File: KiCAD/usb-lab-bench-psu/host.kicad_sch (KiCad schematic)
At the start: 23 parts, among them SW1 SW_Push, U3 ESP32-C3, U4 ZD25WQ32C, Y1 40MHz

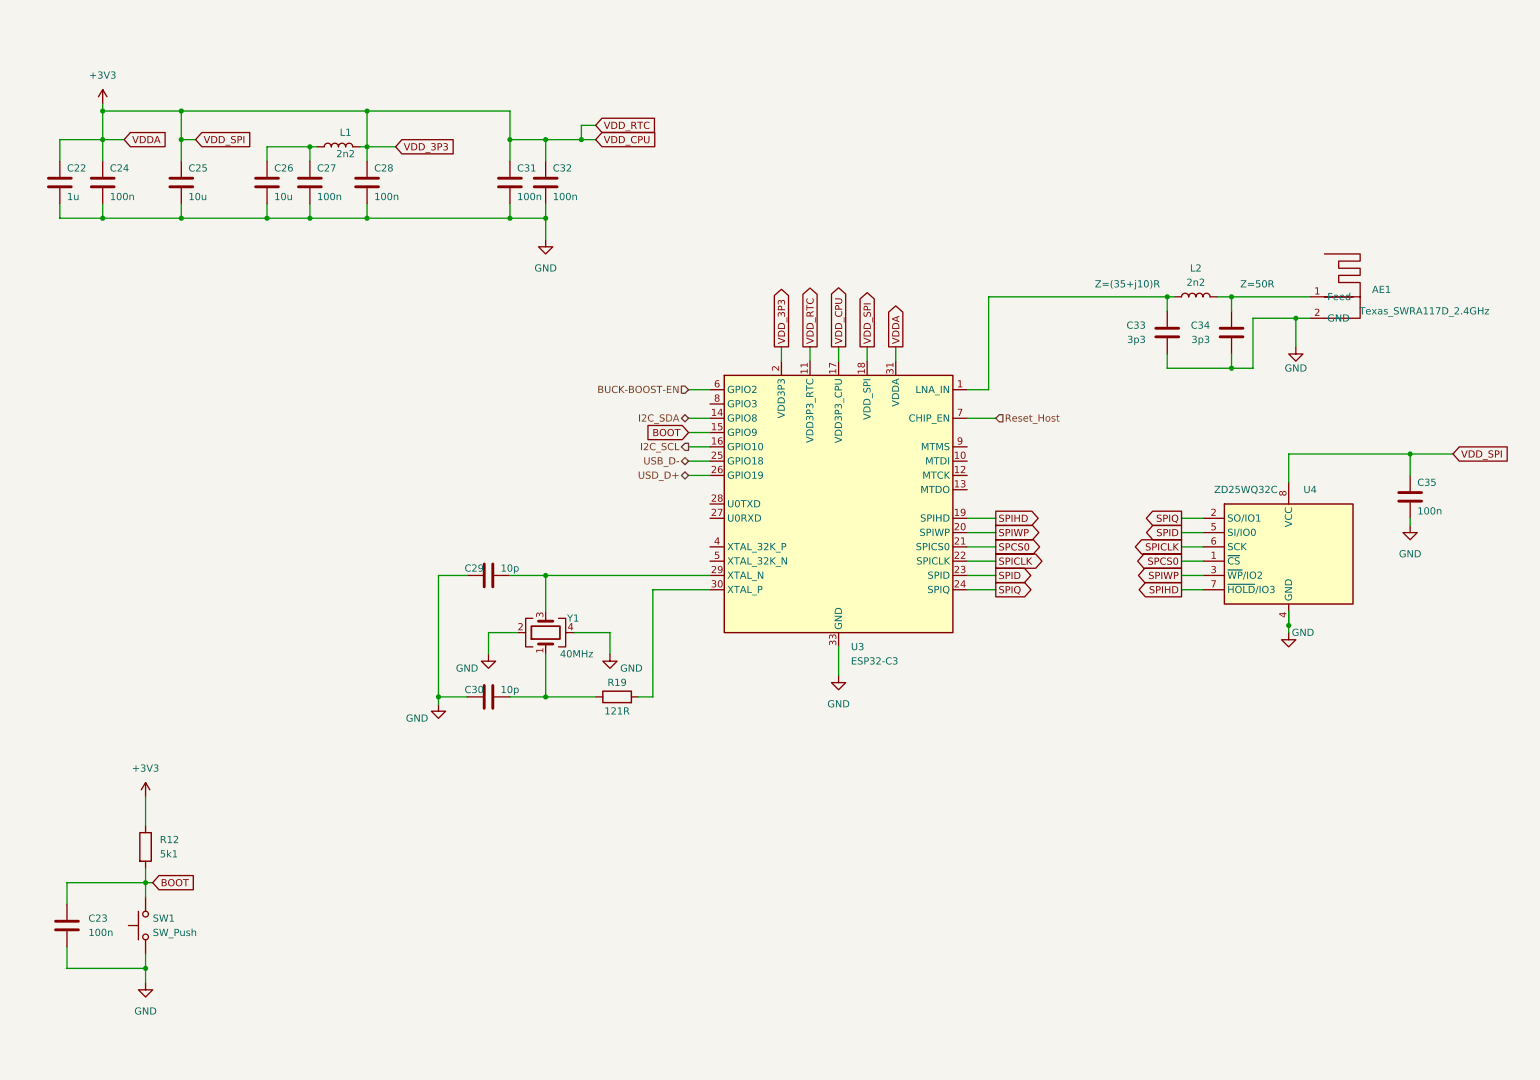
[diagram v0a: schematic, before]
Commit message: Replaced global labels with labels, added measurement circuit, started with io board
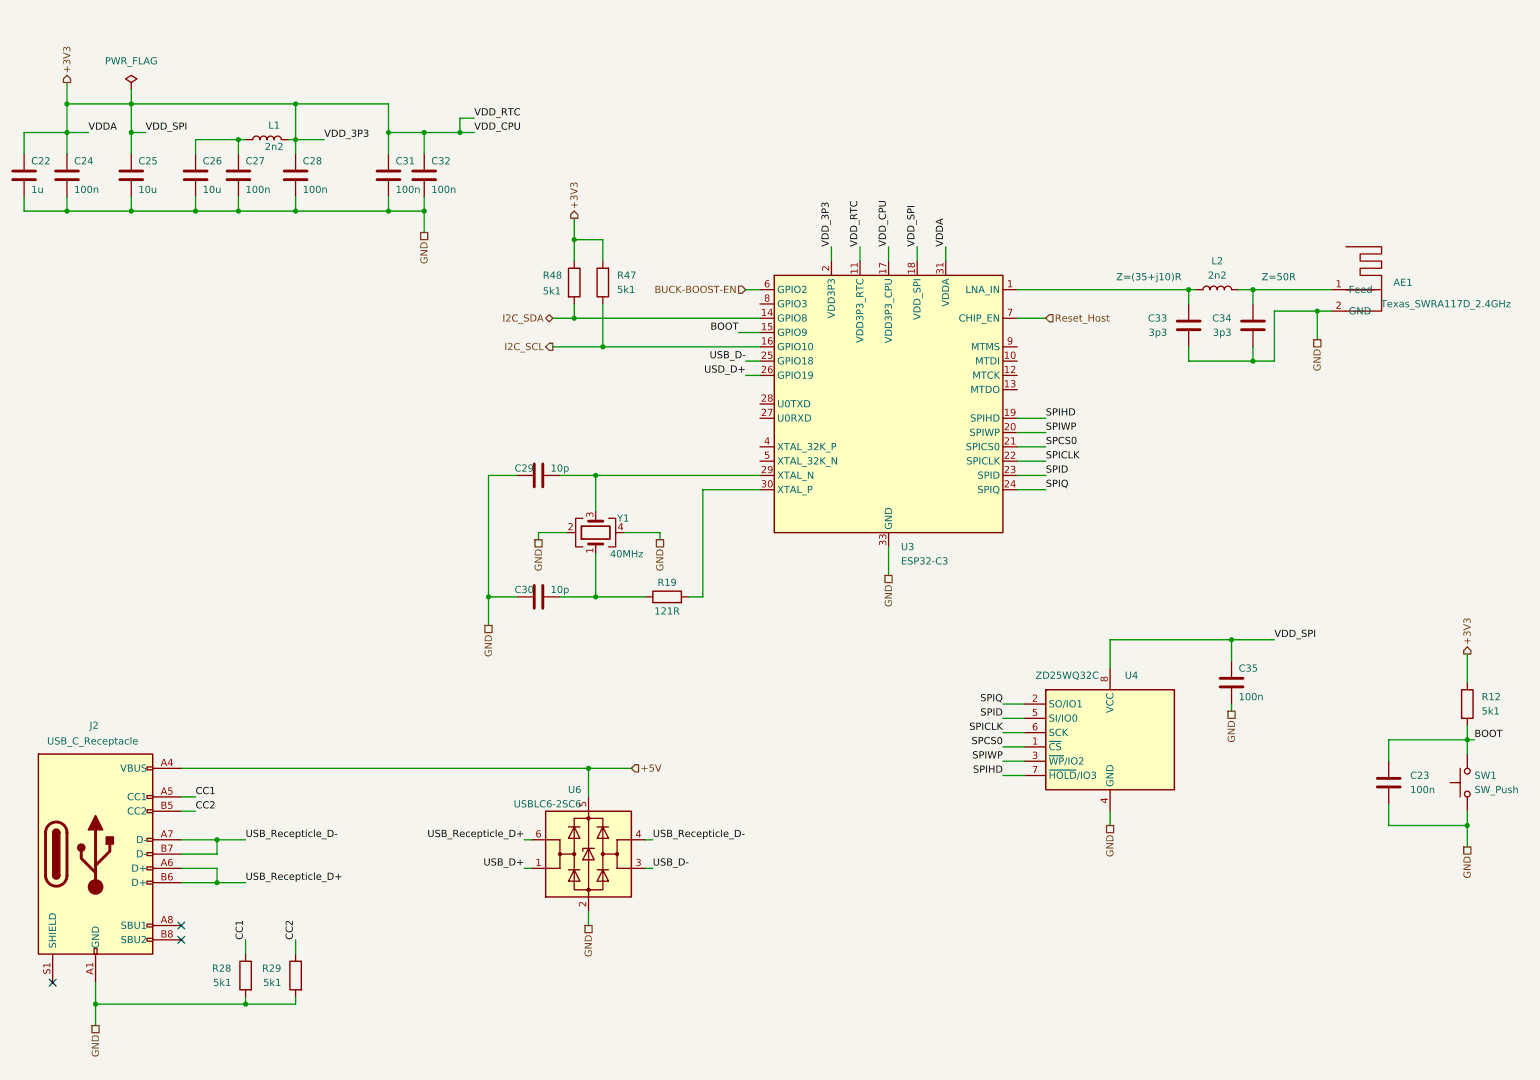
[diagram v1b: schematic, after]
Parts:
- added J2: USB_C_Receptacle, Prj_Connectors_USB:USB_C_Receptacle_SHOU_HAN_TYPE_C_16P_CB1.6_073, symbol Connector:USB_C_Receptacle_USB2.0
- added R28, R29: 5k1, Resistor_SMD:R_0402_1005Metric_Pad0.72x0.64mm_HandSolder, symbol Device:R
- added R47, R48: 5k1, symbol Device:R
- added U6: USBLC6-2SC6, Package_TO_SOT_SMD:SOT-23-6, symbol Power_Protection:USBLC6-2SC6
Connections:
- net +3V3: now also R47.2, R48.1
- net GND: now also J2.A1 (GND), J2.A12 (GND), J2.B1 (GND), J2.B12 (GND), R28.2, R29.2, U6.2 (GND)
- net I2C_SCL: now also R47.1
- net I2C_SDA: now also R48.2
- net USB_D-: now also U6.3 (I/O2)
- new net +5V: J2.A4 (VBUS), J2.A9 (VBUS), J2.B4 (VBUS), J2.B9 (VBUS), U6.5 (VBUS)
- new net CC1: J2.A5 (CC1), R28.1
- new net CC2: J2.B5 (CC2), R29.1
- new net USB_D+: U6.1 (I/O1)
- new net USB_Recepticle_D+: J2.A6 (D+), J2.B6 (D+), U6.6 (I/O1)
- new net USB_Recepticle_D-: J2.A7 (D-), J2.B7 (D-), U6.4 (I/O2)
- no-connect marks 0 -> 3
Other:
- moved on the sheet: AE1, C22, C23, C24, C25, C26, C27, C28, C29, C30, C31, C32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

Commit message: updated GND and supply nets, switched buck-boost-converter
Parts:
- renumbered C24 to C10, C25 to C11, C26 to C12, C27 to C13, C28 to C14, C31 to C15, C32 to C16, C29 to C17, C30 to C18, C33 to C19, C35 to C20, C34 to C21, C23 to C22, C22 to C9, J2 to J4, R28 to R17, R29 to R18, R48 to R19, R47 to R20, R19 to R21, R12 to R22, SW1 to SW2, U6 to U2
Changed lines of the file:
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@@
 		(on_board yes)
 		(dnp no)
-		(property "Reference" "C24"
+		(property "Reference" "C10"
 			(at 25.4 35.56 0)
 			(effects
@@
 			(project "usb-lab-bench-psu"
 				(path "/63928bc9-e618-488a-a687-c6d5597f31d9/445080ef-739d-4817-b509-08b627e2bdcd"
-					(reference "C24")
+					(reference "C10")
 					(unit 1)
 				)
@@
 		(on_board yes)
 		(dnp no)
-		(property "Reference" "C23"
+		(property "Reference" "C22"
 			(at 262.89 144.7799 0)
 			(effects
@@
 			(project "usb-lab-bench-psu"
 				(path "/63928bc9-e618-488a-a687-c6d5597f31d9/445080ef-739d-4817-b509-08b627e2bdcd"
-					(reference "C23")
+					(reference "C22")
 					(unit 1)
 				)
@@
 		(dnp no)
 		(fields_autoplaced yes)
-		(property "Reference" "R12"
+		(property "Reference" "R22"
 			(at 275.59 130.8099 0)
 			(effects
@@
 			(project "usb-lab-bench-psu"
 				(path "/63928bc9-e618-488a-a687-c6d5597f31d9/445080ef-739d-4817-b509-08b627e2bdcd"
-					(reference "R12")
+					(reference "R22")
 					(unit 1)
 				)
@@
 		(dnp no)
 		(fields_autoplaced yes)
-		(property "Reference" "C33"
+		(property "Reference" "C19"
 			(at 219.71 63.4999 0)
 			(effects
@@
 			(project "usb-lab-bench-psu"
 				(path "/63928bc9-e618-488a-a687-c6d5597f31d9/445080ef-739d-4817-b509-08b627e2bdcd"
-					(reference "C33")
+					(reference "C19")
 					(unit 1)
 				)
@@
 		(on_board yes)
 		(dnp no)
-		(property "Reference" "J2"
+		(property "Reference" "J4"
 			(at 28.956 135.89 0)
 			(effects
@@
 			(project "usb-lab-bench-psu"
 				(path "/63928bc9-e618-488a-a687-c6d5597f31d9/445080ef-739d-4817-b509-08b627e2bdcd"
-					(reference "J2")
+					(reference "J4")
 					(unit 1)
 				)
@@
 		(dnp no)
 		(fields_autoplaced yes)
-		(property "Reference" "R29"
+		(property "Reference" "R18"
 			(at 62.23 179.0699 0)
 			(effects
@@
 			(project "usb-lab-bench-psu"
 				(path "/63928bc9-e618-488a-a687-c6d5597f31d9/445080ef-739d-4817-b509-08b627e2bdcd"
-					(reference "R29")
+					(reference "R18")
 					(unit 1)
 				)
@@
 		(on_board yes)
 		(dnp no)
-		(property "Reference" "C27"
+		(property "Reference" "C13"
 			(at 55.88 35.56 0)
 			(effects
@@
 			(project "usb-lab-bench-psu"
 				(path "/63928bc9-e618-488a-a687-c6d5597f31d9/445080ef-739d-4817-b509-08b627e2bdcd"
-					(reference "C27")
+					(reference "C13")
 					(unit 1)
 				)
@@
 		(on_board yes)
 		(dnp no)
-		(property "Reference" "R48"
+		(property "Reference" "R19"
 			(at 108.712 55.88 0)
 			(effects
@@
 			(project "usb-lab-bench-psu"
 				(path "/63928bc9-e618-488a-a687-c6d5597f31d9/445080ef-739d-4817-b509-08b627e2bdcd"
-					(reference "R48")
+					(reference "R19")
 					(unit 1)
 				)
@@
 		(on_board yes)
 		(dnp no)
-		(property "Reference" "C31"
+		(property "Reference" "C15"
 			(at 82.55 35.56 0)
 			(effects
@@
 			(project "usb-lab-bench-psu"
 				(path "/63928bc9-e618-488a-a687-c6d5597f31d9/445080ef-739d-4817-b509-08b627e2bdcd"
-					(reference "C31")
+					(reference "C15")
 					(unit 1)
 				)
@@
 		(on_board yes)
 		(dnp no)
-		(property "Reference" "C25"
+		(property "Reference" "C11"
 			(at 36.83 35.56 0)
 			(effects
@@
 			(project "usb-lab-bench-psu"
 				(path "/63928bc9-e618-488a-a687-c6d5597f31d9/445080ef-739d-4817-b509-08b627e2bdcd"
-					(reference "C25")
+					(reference "C11")
 					(unit 1)
 				)
@@
 		(dnp no)
 		(fields_autoplaced yes)
-		(property "Reference" "C34"
+		(property "Reference" "C21"
 			(at 231.14 63.4999 0)
 			(effects
@@
 			(project "usb-lab-bench-psu"
 				(path "/63928bc9-e618-488a-a687-c6d5597f31d9/445080ef-739d-4817-b509-08b627e2bdcd"
-					(reference "C34")
+					(reference "C21")
 					(unit 1)
 				)
@@
 		(on_board yes)
 		(dnp no)
-		(property "Reference" "U6"
+		(property "Reference" "U2"
 			(at 115.57 147.32 0)
 			(effects
@@
 			(project "usb-lab-bench-psu"
 				(path "/63928bc9-e618-488a-a687-c6d5597f31d9/445080ef-739d-4817-b509-08b627e2bdcd"
-					(reference "U6")
+					(reference "U2")
 					(unit 1)
 				)
@@
 		(dnp no)
 		(fields_autoplaced yes)
-		(property "Reference" "R28"
+		(property "Reference" "R17"
 			(at 53.34 179.0699 0)
 			(effects
@@
 			(project "usb-lab-bench-psu"
 				(path "/63928bc9-e618-488a-a687-c6d5597f31d9/445080ef-739d-4817-b509-08b627e2bdcd"
-					(reference "R28")
+					(reference "R17")
 					(unit 1)
 				)
@@
 		(on_board yes)
 		(dnp no)
-		(property "Reference" "SW1"
+		(property "Reference" "SW2"
 			(at 274.32 144.78 90)
 			(effects
@@
 			(project "usb-lab-bench-psu"
 				(path "/63928bc9-e618-488a-a687-c6d5597f31d9/445080ef-739d-4817-b509-08b627e2bdcd"
-					(reference "SW1")
+					(reference "SW2")
 					(unit 1)
 				)
@@
 		(on_board yes)
 		(dnp no)
-		(property "Reference" "C30"
+		(property "Reference" "C18"
 			(at 105.41 111.76 90)
 			(effects
@@
 			(project "usb-lab-bench-psu"
 				(path "/63928bc9-e618-488a-a687-c6d5597f31d9/445080ef-739d-4817-b509-08b627e2bdcd"
-					(reference "C30")
+					(reference "C18")
 					(unit 1)
 				)
@@
 		(on_board yes)
 		(dnp no)
-		(property "Reference" "C26"
+		(property "Reference" "C12"
 			(at 48.26 35.56 0)
 			(effects
@@
 			(project "usb-lab-bench-psu"
 				(path "/63928bc9-e618-488a-a687-c6d5597f31d9/445080ef-739d-4817-b509-08b627e2bdcd"
-					(reference "C26")
+					(reference "C12")
 					(unit 1)
 				)
@@
 		(on_board yes)
 		(dnp no)
-		(property "Reference" "R19"
+		(property "Reference" "R21"
 			(at 130.81 110.49 90)
 			(effects
@@
 			(project "usb-lab-bench-psu"
 				(path "/63928bc9-e618-488a-a687-c6d5597f31d9/445080ef-739d-4817-b509-08b627e2bdcd"
-					(reference "R19")
+					(reference "R21")
 					(unit 1)
 				)
@@
 		(on_board yes)
 		(dnp no)
-		(property "Reference" "C32"
+		(property "Reference" "C16"
 			(at 88.9 35.56 0)
 			(effects
@@
 			(project "usb-lab-bench-psu"
 				(path "/63928bc9-e618-488a-a687-c6d5597f31d9/445080ef-739d-4817-b509-08b627e2bdcd"
-					(reference "C32")
+					(reference "C16")
 					(unit 1)
 				)
@@
 		(on_board yes)
 		(dnp no)
-		(property "Reference" "C28"
+		(property "Reference" "C14"
 			(at 66.04 35.56 0)
 			(effects
@@
 			(project "usb-lab-bench-psu"
 				(path "/63928bc9-e618-488a-a687-c6d5597f31d9/445080ef-739d-4817-b509-08b627e2bdcd"
-					(reference "C28")
+					(reference "C14")
 					(unit 1)
 				)
@@
 		(on_board yes)
 		(dnp no)
-		(property "Reference" "C29"
+		(property "Reference" "C17"
 			(at 105.41 90.17 90)
 			(effects
@@
 			(project "usb-lab-bench-psu"
 				(path "/63928bc9-e618-488a-a687-c6d5597f31d9/445080ef-739d-4817-b509-08b627e2bdcd"
-					(reference "C29")
+					(reference "C17")
 					(unit 1)
 				)
@@
 		(on_board yes)
 		(dnp no)
-		(property "Reference" "C35"
+		(property "Reference" "C20"
 			(at 232.41 125.73 0)
 			(effects
@@
 			(project "usb-lab-bench-psu"
 				(path "/63928bc9-e618-488a-a687-c6d5597f31d9/445080ef-739d-4817-b509-08b627e2bdcd"
-					(reference "C35")
+					(reference "C20")
 					(unit 1)
 				)
@@
 		(on_board yes)
 		(dnp no)
-		(property "Reference" "C22"
+		(property "Reference" "C9"
 			(at 17.78 35.56 0)
 			(effects
@@
 			(project "usb-lab-bench-psu"
 				(path "/63928bc9-e618-488a-a687-c6d5597f31d9/445080ef-739d-4817-b509-08b627e2bdcd"
-					(reference "C22")
+					(reference "C9")
 					(unit 1)
 				)
@@
 		(dnp no)
 		(fields_autoplaced yes)
-		(property "Reference" "#FLG015"
+		(property "Reference" "#FLG06"
 			(at 35.56 20.955 0)
 			(effects
@@
 			(project ""
 				(path "/63928bc9-e618-488a-a687-c6d5597f31d9/445080ef-739d-4817-b509-08b627e2bdcd"
-					(reference "#FLG015")
+					(reference "#FLG06")
 					(unit 1)
 				)
@@
 		(dnp no)
 		(fields_autoplaced yes)
-		(property "Reference" "R47"
+		(property "Reference" "R20"
 			(at 121.92 55.8799 0)
 			(effects
@@
 			(project ""
 				(path "/63928bc9-e618-488a-a687-c6d5597f31d9/445080ef-739d-4817-b509-08b627e2bdcd"
-					(reference "R47")
-					(unit 1)
-				)
+					(reference "R20")
+					(unit 1)
+				)
